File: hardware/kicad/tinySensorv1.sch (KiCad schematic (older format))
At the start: 32 parts, among them J1 RADIO, J10 CR2032 socket, J11 AAA socket, J12 AA Socket, J13 RAW IN, J2 DCDC converter, J3 BMP/BME breakout, J4 PWM out, J5 OneWire sensor, J6 ISP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

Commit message: feat: Last enhancements from hardware testing
* Full LM35 support: <0 temp with diode support
* 433Mhz emitter is powered by SENSOR_VCC
* Enhanced layout
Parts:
- removed C3: 1u, Capacitor_THT:CP_Radial_D4.0mm_P1.50mm, symbol Device:CP1
- added D2, D3: 1N4001, Diode_THT:D_DO-34_SOD68_P2.54mm_Vertical_AnodeUp, symbol Diode:1N4001
- added JP3: Ground ref, Jumper:SolderJumper-3_P1.3mm_Open_Pad1.0x1.5mm_NumberLabels, symbol Jumper:SolderJumper_3_Open
- added R5, R7: 1k, Resistor_THT:R_Axial_DIN0204_L3.6mm_D1.6mm_P7.62mm_Horizontal, symbol Device:R
- R4: value 75R -> 18k
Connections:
- net labels added: Battery_Checker_Probe, OneWire_and_analog_bias
- net labels removed: OneWire
- wire segments 93 -> 108
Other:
- note added: "Battery sensor voltage divider"
- note removed: "Optional RC filter for LM35 sensor"
- moved on the sheet: D1, JP1, R1

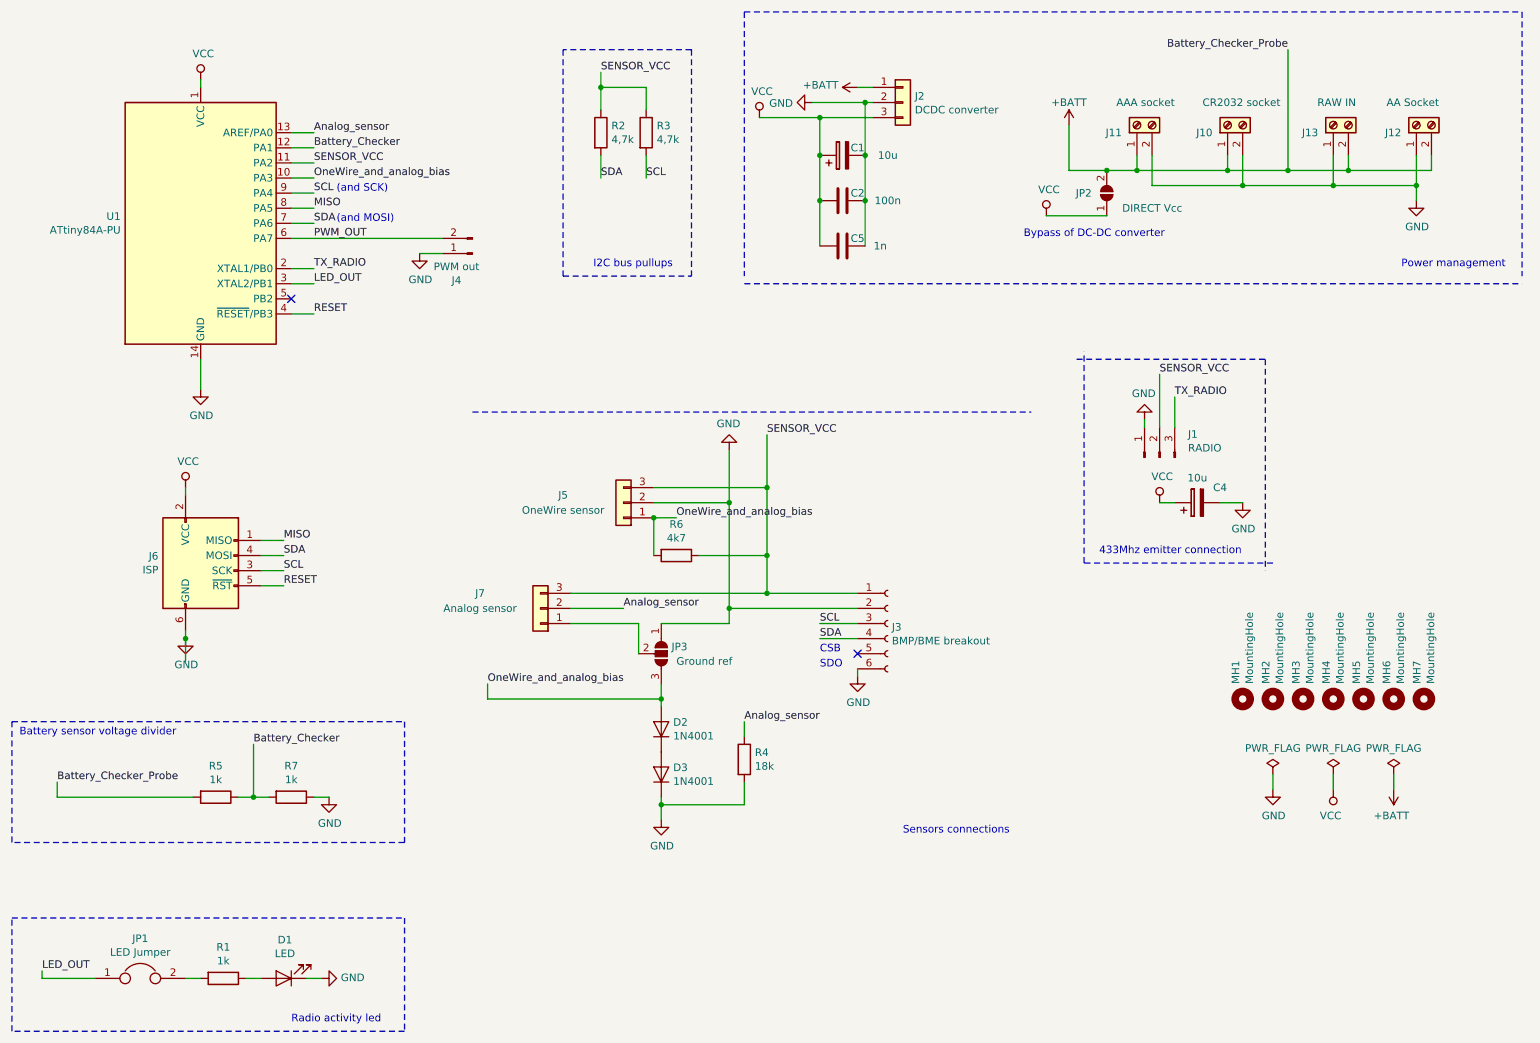
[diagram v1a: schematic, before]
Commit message: feat: Allow shutdown of DCDC stepup
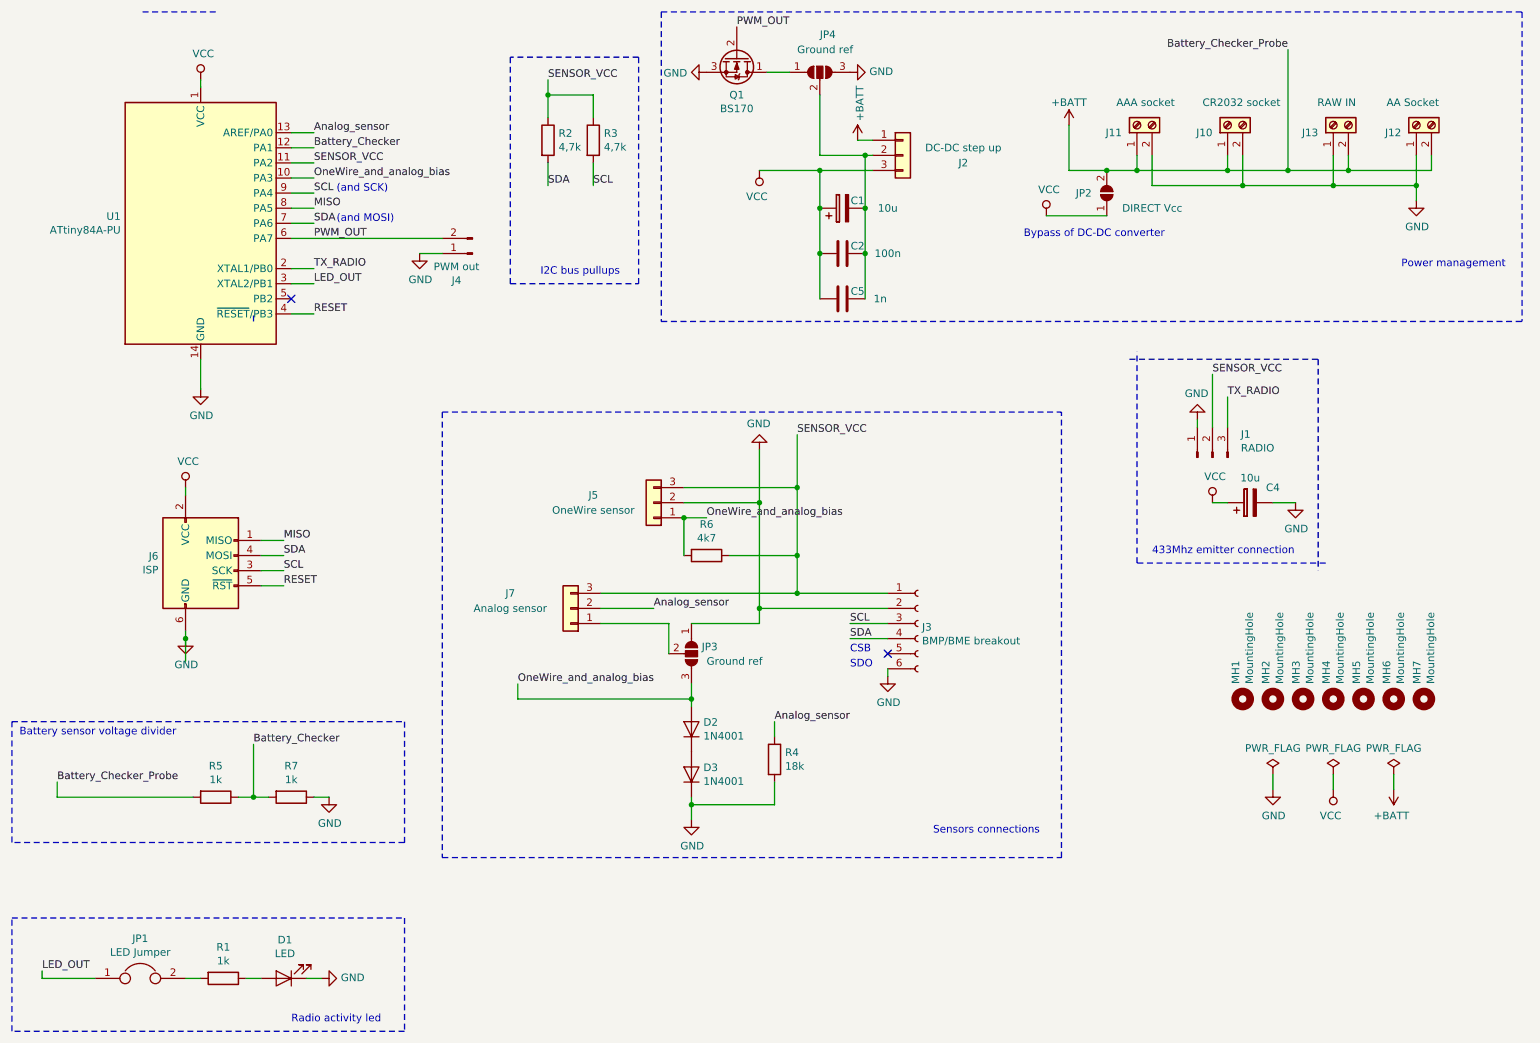
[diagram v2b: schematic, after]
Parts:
- added JP4: Ground ref, Jumper:SolderJumper-3_P1.3mm_Open_Pad1.0x1.5mm_NumberLabels, symbol Jumper:SolderJumper_3_Open
- added Q1: BS170, Package_TO_SOT_THT:TO-92_Inline, symbol Transistor_FET:BS170
- J2: value DCDC converter -> DC-DC step up; footprint TinySensor lib:DC-DC_0.9v-3.3v_to_3.3v -> Connector_PinHeader_2.54mm:PinHeader_1x03_P2.54mm_Vertical
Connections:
- net GND: now also JP4.3 (B), Q1.3 (S); no longer C1.2, C2.1, C5.1, J2.2 (Pin_2)
- net PWM_OUT: now also Q1.2 (G)
- new net: C1.2, C2.1, C5.1, J2.2 (Pin_2), JP4.2 (C)
- new net: JP4.1 (A), Q1.1 (D)
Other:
- moved on the sheet: C1, C2, C4, C5, D2, D3, J1, J3, J5, J7, JP3, R2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
